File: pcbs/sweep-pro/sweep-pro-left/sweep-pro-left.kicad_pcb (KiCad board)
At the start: 2 copper layers, 115 x 86.7 mm, 50 parts, among them J1 Conn_01x04_Female, J2 Conn_01x04_Female, J3 expantion1, SW1 SW_PUSH-kbd, SW10 SW_PUSH-kbd, SW11 SW_PUSH-kbd, SW12 SW_PUSH-kbd, SW13 SW_PUSH-kbd, SW14 SW_PUSH-kbd, SW15 SW_PUSH-kbd, SW16 SW_PUSH-kbd, SW17 SW_PUSH-kbd, SW2 SW_PUSH-kbd, SW3 SW_PUSH-kbd, SW4 SW_PUSH-kbd, SW5 SW_PUSH-kbd, SW6 SW_PUSH-kbd, SW7 SW_PUSH-kbd, SW8 SW_PUSH-kbd, SW9 SW_PUSH-kbd, U1 ProMicro-kbd

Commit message: backup
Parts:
- moved Encoder1 0.35 mm to (199.0, 93.1)
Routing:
- net col5: track 85.4 -> 87.1 mm

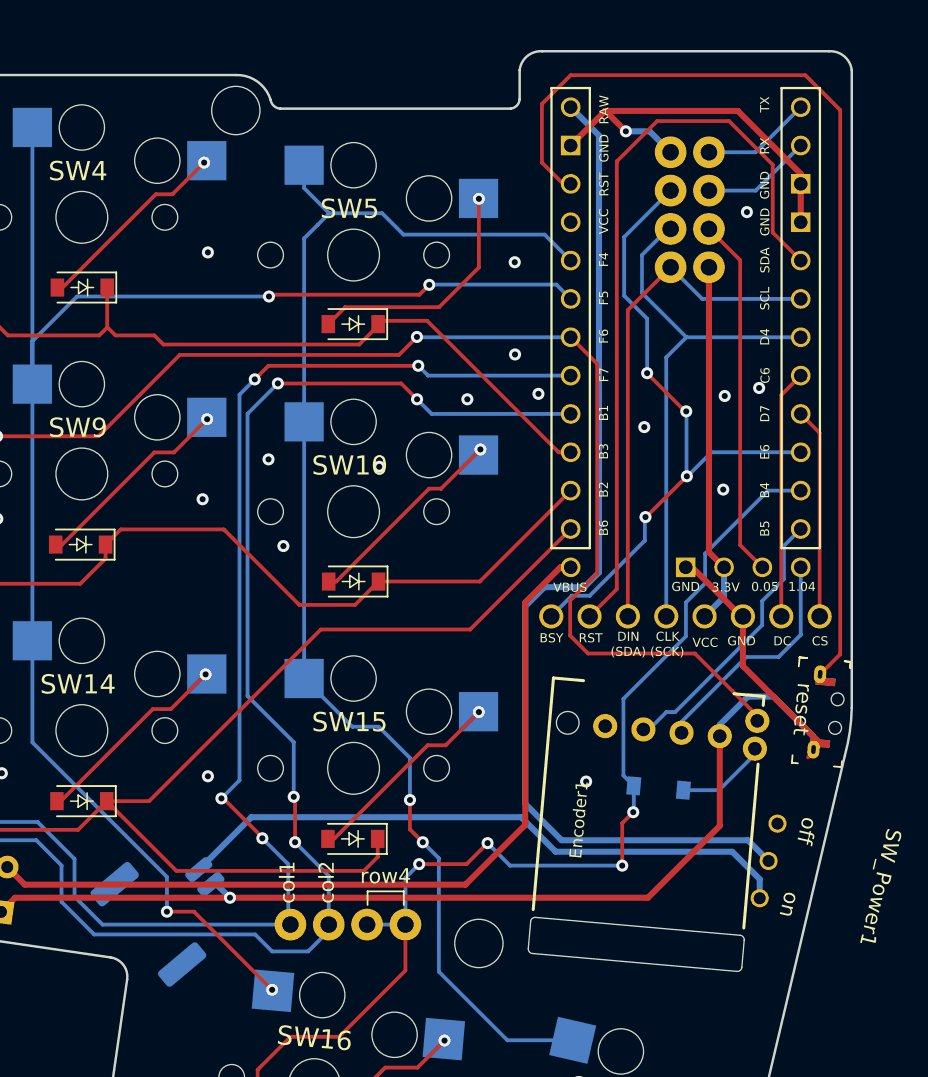
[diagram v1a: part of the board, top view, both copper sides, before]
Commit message: sweepro v2
1. add three expansion ports (pogopin connection)
2. remev battery extra port
3. use nrfmacro-lite partial footprint
4. new power switch
5. re-position reset button
6. seperate board for left and right split
7. more symmetric layout of the encoders
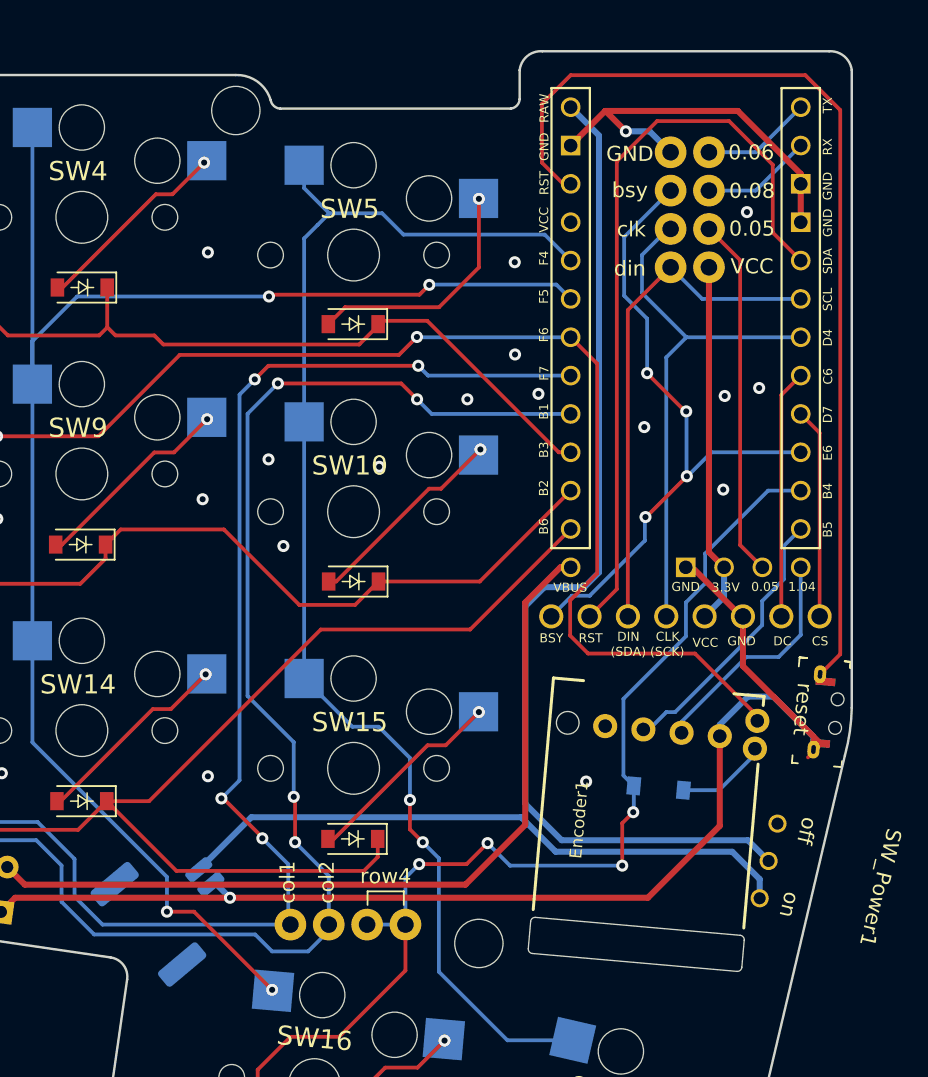
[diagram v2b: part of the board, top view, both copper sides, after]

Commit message: backup
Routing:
- net GND: vias 40 -> 35
